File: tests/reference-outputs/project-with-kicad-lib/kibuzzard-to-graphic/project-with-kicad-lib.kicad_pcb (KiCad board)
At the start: 2 copper layers, 20.3 x 9.7 mm, 7 parts, among them U1 ADS1115IDGS

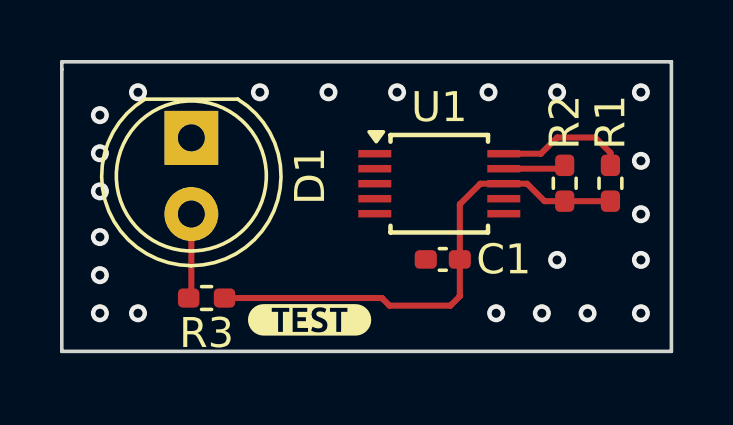
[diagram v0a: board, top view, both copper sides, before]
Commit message: [#63381] Add kibuzzard-to-graphic command
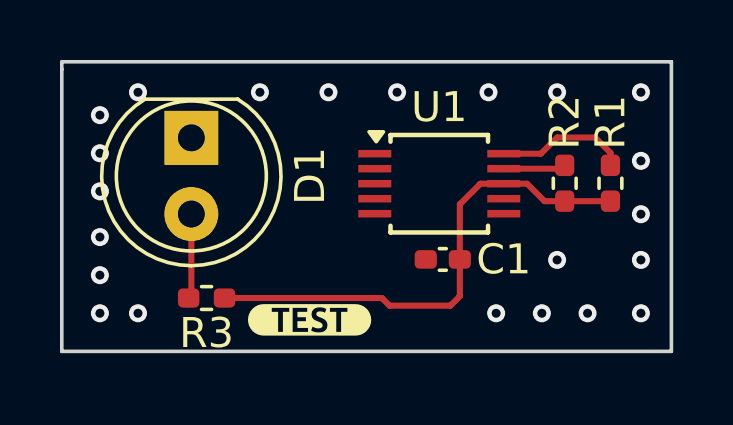
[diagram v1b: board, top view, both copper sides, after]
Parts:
- removed kibuzzard-66D96414: G***, kibuzzard-66D96414
- C1: footprint (none) -> Capacitor_SMD:C_0402_1005Metric_Pad0.74x0.62mm_HandSolder
- D1: footprint (none) -> LED_THT:LED_D5.0mm
- R1, R2, R3: footprint (none) -> Resistor_SMD:R_0402_1005Metric_Pad0.72x0.64mm_HandSolder
